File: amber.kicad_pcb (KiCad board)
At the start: 2 copper layers, 118.9 x 112.3 mm, 46 parts, among them J1 SJ-43504-SMT-TR

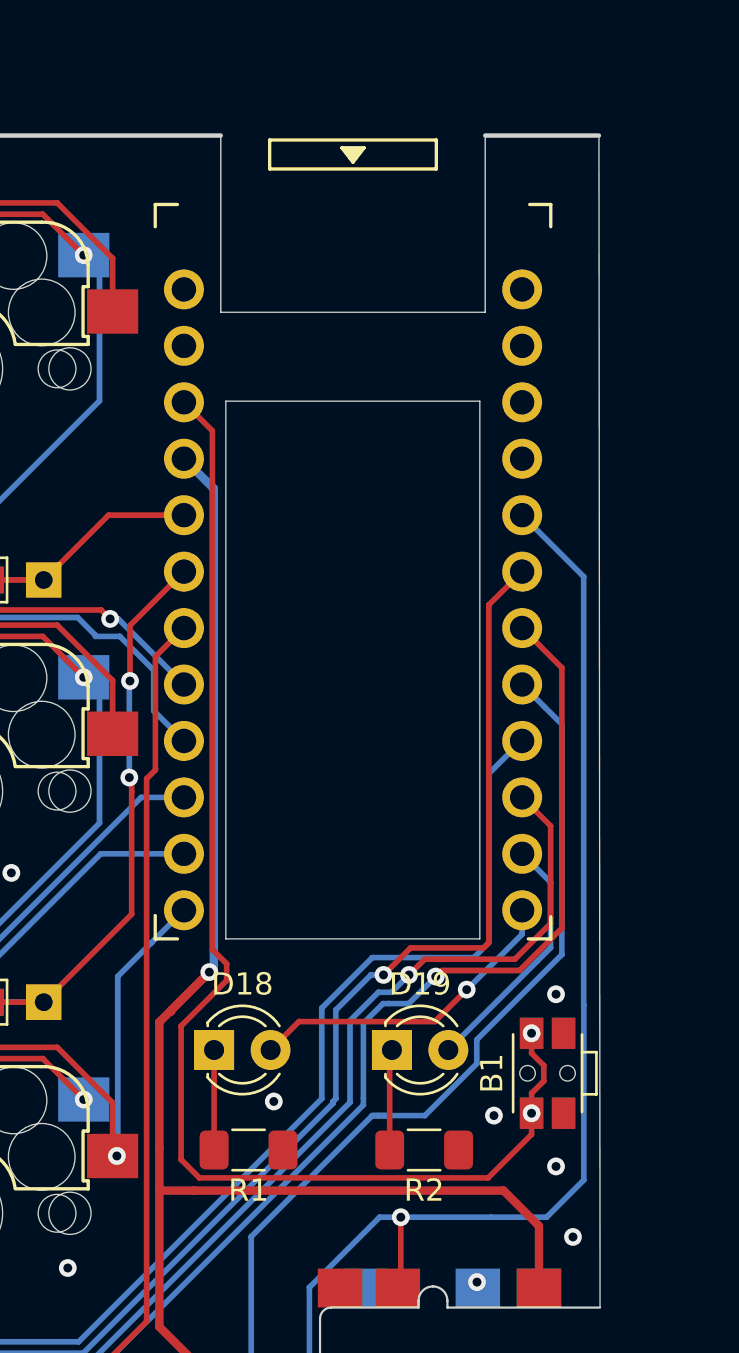
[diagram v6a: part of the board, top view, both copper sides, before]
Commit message: Make a reversible MCU socket using jumpers
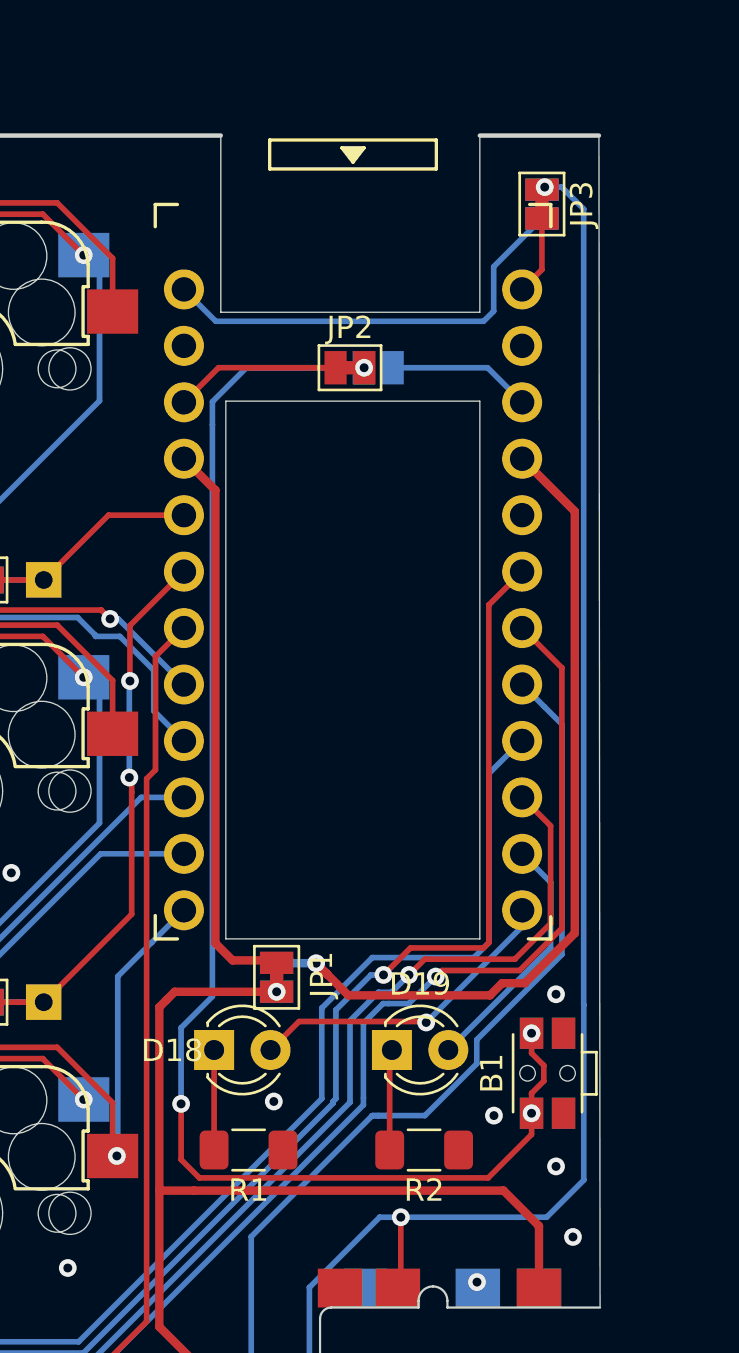
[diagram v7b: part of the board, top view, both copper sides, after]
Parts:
- added JP1: Jumper_2_Bridged, Jumper:SolderJumper-2_P1.3mm_Bridged_Pad1.0x1.5mm, F.Cu at (91.3, -9.27)
- added JP2: Jumper_2_Bridged, Jumper:SolderJumper-2_P1.3mm_Bridged_Pad1.0x1.5mm, F.Cu at (94.6, -36.7)
- added JP3: Jumper_2_Bridged, Jumper:SolderJumper-2_P1.3mm_Bridged_Pad1.0x1.5mm, F.Cu at (103.3, -44.1)
- added JP4: Jumper_2_Open, Jumper:SolderJumper-2_P1.3mm_Open_Pad1.0x1.5mm, B.Cu at (103.3, -44.1)
- added JP5: Jumper_2_Open, Jumper:SolderJumper-2_P1.3mm_Open_Pad1.0x1.5mm, B.Cu at (95.9, -36.7)
- added JP6: Jumper_2_Open, Jumper:SolderJumper-2_P1.3mm_Open_Pad1.0x1.5mm, B.Cu at (91.3, -9.27)
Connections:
- C1 pad 2: Net-(C1-Pad2) -> GND
- C1 pad 21: VCC -> Net-(C1-Pad21)
- C1 pad 22: RST -> Net-(C1-Pad22)
- C1 pad 3: GND -> Net-(C1-Pad3)
- C1 pad 4: GND -> Net-(C1-Pad4)
- C1 pad 5: Serial -> Net-(C1-Pad5)
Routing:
- net Net-(C1-Pad4): track 0.00 -> 37.7 mm, vias 0 -> 1
- net Net-(C1-Pad21): track 0.00 -> 25.5 mm
- net VCC: track 89.6 -> 66.4 mm
- net Net-(C1-Pad24): track 0.00 -> 19.8 mm
- net Serial: track 62.8 -> 77.5 mm, vias 1 -> 2
- net Net-(C1-Pad22): track 0.00 -> 7.47 mm
- net Net-(C1-Pad3): track 0.00 -> 6.47 mm
- net RST: track 57.7 -> 64.1 mm, vias 2 -> 4
- net Net-(C1-Pad1): track 0.00 -> 3.56 mm
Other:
- outline, holes or cut-outs redrawn

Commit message: Fix the encoder/switch footprint
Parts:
- removed D15: 1N4148, amber:Diode_THT7.6_SOD123
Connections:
- S15 pad S2: Net-(D15-Pad2) -> RE
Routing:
- net Net-(D15-Pad2): track 21.2 -> 0.00 mm
- net CE: track 86.1 -> 98.3 mm, vias 1 -> 2
- net RE: track 69.4 -> 72.5 mm, vias 0 -> 1
